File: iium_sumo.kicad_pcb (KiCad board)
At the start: 2 copper layers, 120.8 x 64.6 mm, 51 parts, among them J1 I2C_VL53_1, J10 Cytron MD, J11 Cytron Start Module, J12 Conn_01x05, J13 Conn_01x05, J14 Conn_01x05, J15 Conn_01x15_Pin, J16 Conn_01x02_Pin, J17 Conn_01x02_Pin, J2 I2C_VL53_2, J3 I2C_VL53_3, J4 I2C_VL53_4, J5 I2C_VL53_5, J6 IR_1, J7 IR_2, J8 IR_3, J9 IR_4, SW1 SW_SPST, SW2 SW_SPST, U1 TPS54360DDA, U4 Black Pill v2, U5 LM3940

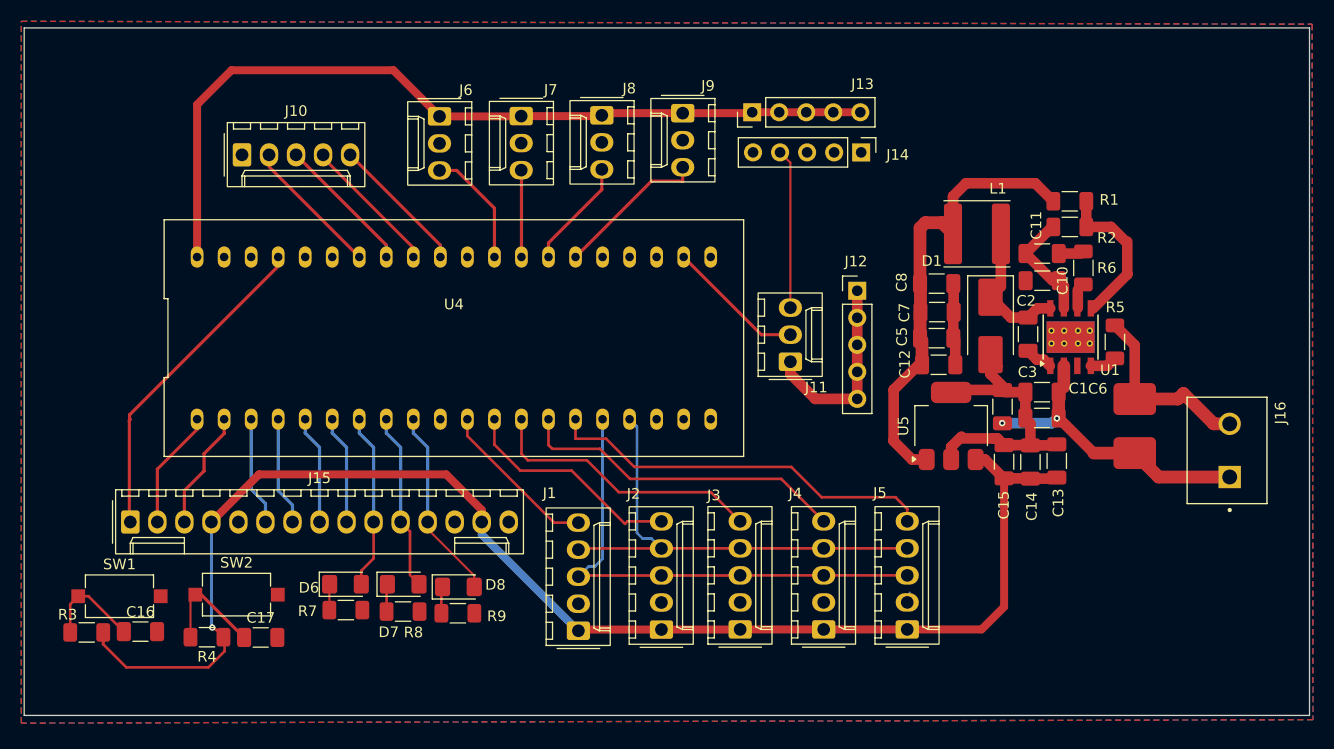
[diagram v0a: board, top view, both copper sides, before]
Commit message: Add UART interface and update PCB design
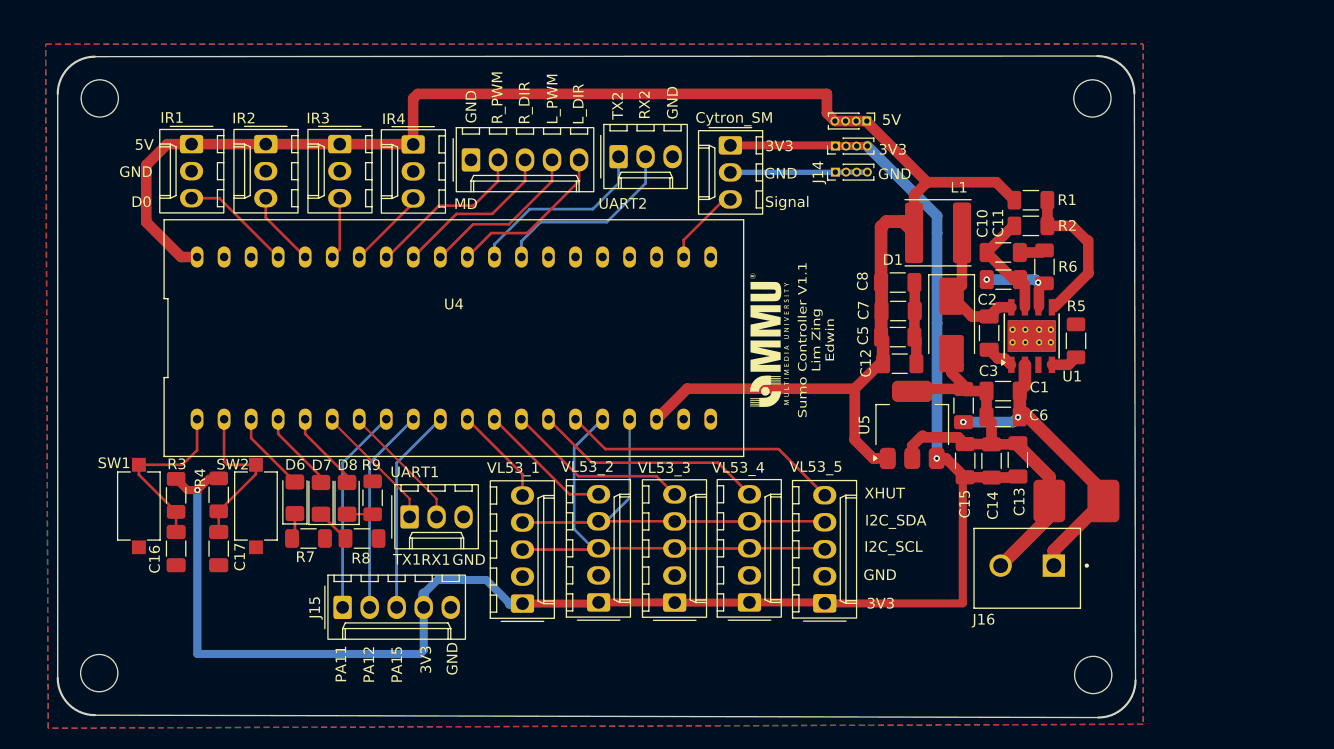
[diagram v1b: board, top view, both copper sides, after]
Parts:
- removed J13: Conn_01x05, Connector_PinHeader_2.54mm:PinHeader_1x05_P2.54mm_Vertical
- added 5V: Conn_01x04, Connector_PinHeader_1.00mm:PinHeader_1x04_P1.00mm_Vertical, F.Cu at (172.4, 66.3)
- added G***: LOGO, shooter_foot_library:mmu_logo, F.Cu at (163.2, 86.9)
- added REF**: MountingHole_3.5mm, MountingHole:MountingHole_3.5mm, F.Cu at (193.6, 64.2)
- added REF**: MountingHole_3.5mm, MountingHole:MountingHole_3.5mm, F.Cu at (100.3, 118.2)
- added REF**: MountingHole_3.5mm, MountingHole:MountingHole_3.5mm, F.Cu at (100.3, 64.2)
- added REF**: MountingHole_3.5mm, MountingHole:MountingHole_3.5mm, F.Cu at (193.7, 118.4)
- added UART1: UART1, Connector_Molex:Molex_KK-254_AE-6410-03A_1x03_P2.54mm_Vertical, F.Cu at (129.4, 103.5)
- added UART2: UART2, Connector_Molex:Molex_KK-254_AE-6410-03A_1x03_P2.54mm_Vertical, F.Cu at (149.1, 69.7)
- J12, J14: value Conn_01x05 -> Conn_01x04; footprint Connector_PinHeader_2.54mm:PinHeader_1x05_P2.54mm_Vertical -> Connector_PinHeader_1.00mm:PinHeader_1x04_P1.00mm_Vertical
- J15: value Conn_01x15_Pin -> EXTRA1; footprint Connector_Molex:Molex_KK-254_AE-6410-15A_1x15_P2.54mm_Vertical -> Connector_Molex:Molex_KK-254_AE-6410-05A_1x05_P2.54mm_Vertical
- moved IR4 25.5 mm to (129.8, 68.5)
- moved IR3 24.8 mm to (122.9, 68.5)
- moved IR2 24.1 mm to (115.9, 68.5)
- moved IR1 23.4 mm to (109.0, 68.5)
- moved J16 21.9 mm to (187.5, 108.1), turned to 180 degrees
- moved MD 21.5 mm to (135.2, 70.0)
- moved J15 21.5 mm to (123.1, 112.0)
- moved Cytron_SM 21.1 mm to (159.6, 68.6), turned to -90 degrees
- moved R3 15.4 mm to (107.5, 101.5), turned to -90 degrees
- moved J12 13.7 mm to (169.4, 68.7), turned to 90 degrees
- moved R9 13.5 mm to (126.0, 101.7), turned to -90 degrees
- moved R4 13.4 mm to (111.5, 101.5), turned to -90 degrees
- moved D8 13.4 mm to (123.6, 101.8), turned to 90 degrees
- moved D7 11.2 mm to (121.1, 101.8), turned to 90 degrees
- moved D6 9.41 mm to (118.7, 101.7), turned to 90 degrees
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- renumbered J11 to Cytron_SM, J6 to IR1, J7 to IR2, J8 to IR3, J9 to IR4, J10 to MD, J1 to VL53_1, J2 to VL53_2, J3 to VL53_3, J4 to VL53_4, J5 to VL53_5
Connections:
- C16 pad 1: /PB14 -> /PB12
- C17 pad 1: /PB15 -> /PB13
- Cytron_SM pad 2: /SM_Signal -> GND
- Cytron_SM pad 3: GND -> /SM_Signal
- D6 pad 2: /PA10 -> /PB14
- D7 pad 2: /PA11 -> /PB15
- D8 pad 2: /PA12 -> /PA8
- J15 pad 1: /PB10 -> /PA11
- J15 pad 2: /PB12 -> /PA12
- J15 pad 3: /PB13 -> /PA15
- R3 pad 2: /PB14 -> /PB12
- R4 pad 2: /PB15 -> /PB13
- SW1 pad 1: /PB14 -> /PB12
- SW2 pad 1: /PB15 -> /PB13
- U4 pad 10: unconnected-(U4-PA15-Pad10) -> /PA15
- U4 pad 18: unconnected-(U4-+5V-Pad18) -> +5V
- U4 pad 19: unconnected-(U4-GND-Pad19) -> GND
- U4 pad 26: /IR4_D0 -> unconnected-(U4-PA0-Pad26)
- U4 pad 27: /IR3_D0 -> unconnected-(U4-PA1-Pad27)
- U4 pad 28: /IR2_D0 -> /RX2
- U4 pad 29: /IR1_D0 -> /TX2
- U4 pad 30: unconnected-(U4-PA4-Pad30) -> /LEFT_DIR
- U4 pad 31: /LEFT_DIR -> /LEFT_PWM
- U4 pad 32: /LEFT_PWM -> /RIGHT_DIR
- U4 pad 33: /RIGHT_DIR -> /RIGHT_PWM
- U4 pad 34: /RIGHT_PWM -> /IR4_D0
- U4 pad 35: unconnected-(U4-PB1-Pad35) -> /IR3_D0
- U4 pad 36: unconnected-(U4-PB2-Pad36) -> /IR2_D0
- U4 pad 37: /PB10 -> /IR1_D0
- U4 pad 6: /PA9 -> /TX1
- U4 pad 7: /PA10 -> /RX1
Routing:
- net +5V: track 123.6 -> 158.1 mm
- net /PB10: track 30.8 -> 0.00 mm
- net /PA15: track 0.00 -> 19.4 mm
- net /RX2: track 0.00 -> 17.9 mm
- net /TX2: track 0.00 -> 17.7 mm
- net /PA10: track 16.5 -> 0.00 mm
- net +3V3: track 150.9 -> 164.8 mm, vias 3 -> 2
- net /PB15: track 20.7 -> 7.61 mm
- net /TX1: track 0.00 -> 12.2 mm
- net /RX1: track 0.00 -> 12.2 mm
- net /PB14: track 19.6 -> 8.15 mm
- net /XHUT5: track 36.9 -> 26.4 mm
- net /PA9: track 10.2 -> 0.00 mm
- net /XHUT4: track 31.3 -> 21.8 mm
- net GND: track 86.1 -> 77.0 mm
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- added copper zone on B.Cu, net GND
- added copper zone on F.Cu, net GND
- removed copper zone on B.Cu, net (none)
- removed copper zone on F.Cu, net (none)
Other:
- board size 120.8 x 64.6 mm -> 101.3 x 62.2 mm
- board text added: "3V3"
- board text added: "5V"
- board text added: "D0"
- board text added: "GND"
- board text added: "I2C_SCL"
- board text added: "I2C_SDA"
- board text added: "L_DIR"
- board text added: "L_PWM"
- board text added: "PA11"
- board text added: "PA12"
- board text added: "PA15"
- board text added: "RX1"
- board text added: "RX2"
- board text added: "R_DIR"
- board text added: "R_PWM"
- board text added: "Signal"
- board text added: "Sumo Controller V1.1 Lim Zing Edwin"
- board text added: "TX1"
- board text added: "TX2"
- board text added: "XHUT"
